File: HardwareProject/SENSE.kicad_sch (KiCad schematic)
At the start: 16 parts, among them U16 INA241A3xDDF, U17 INA241A3xDDF, U20 SGM8551XN, U21 SGM8551XN

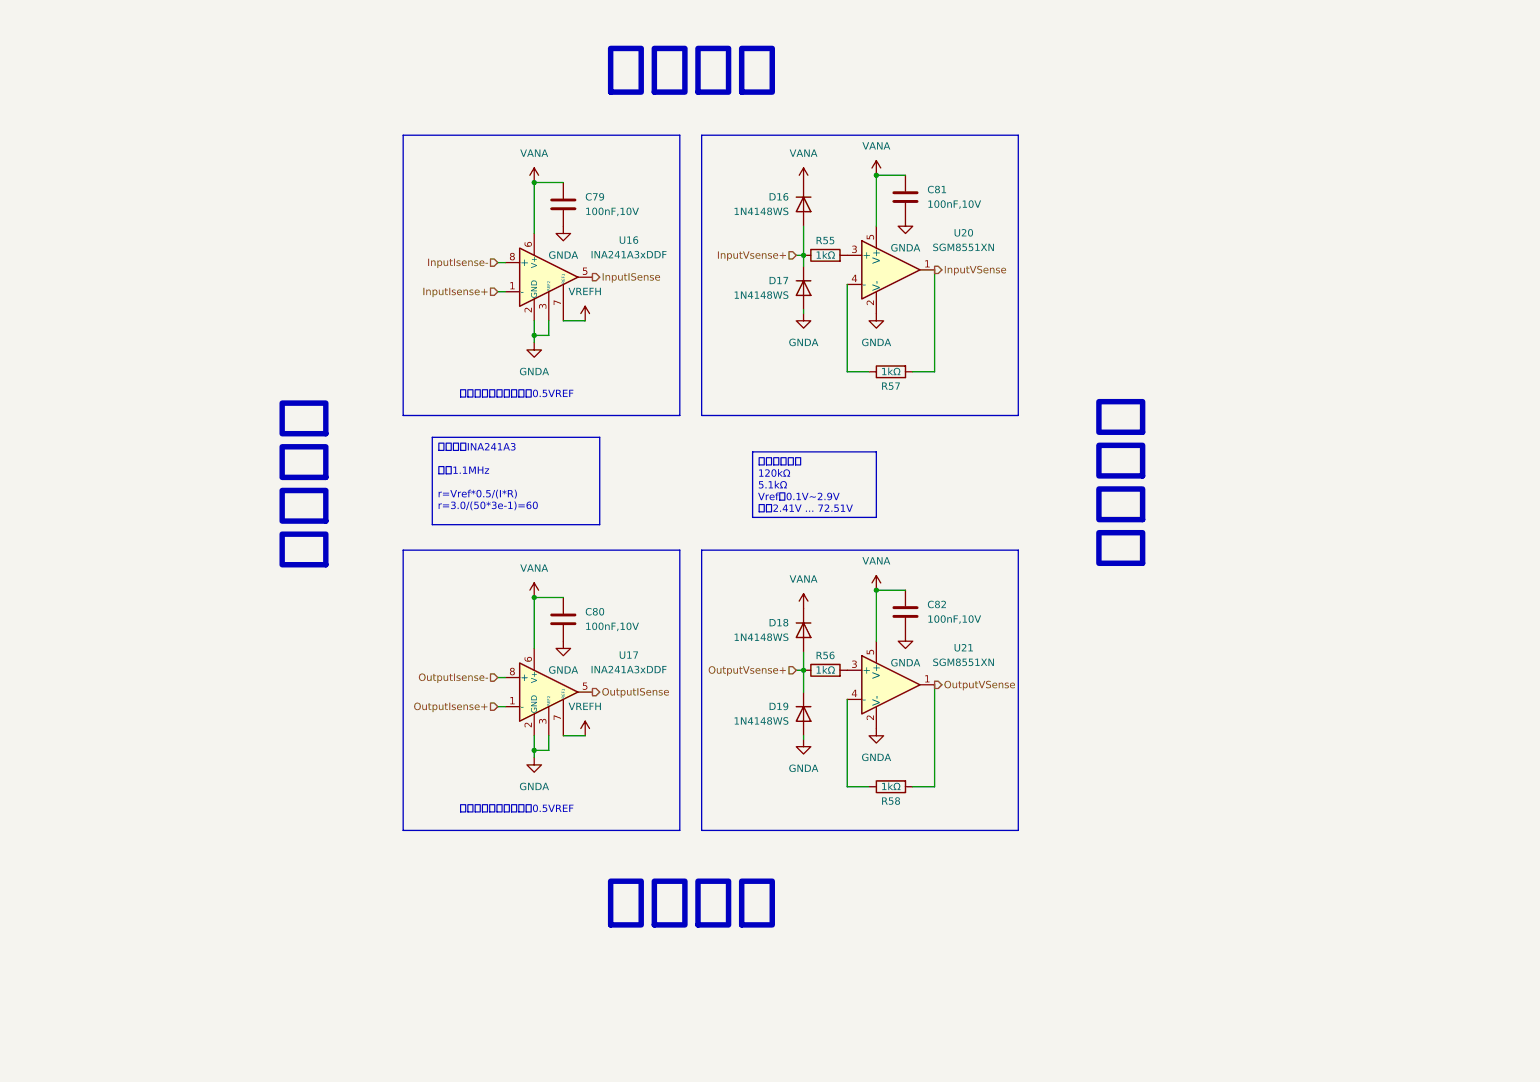
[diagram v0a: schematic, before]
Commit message: 修改了UCC27211A封装，此芯片此前的封装均错误 修改了采样线布局，为SAR ADC加入前置RC
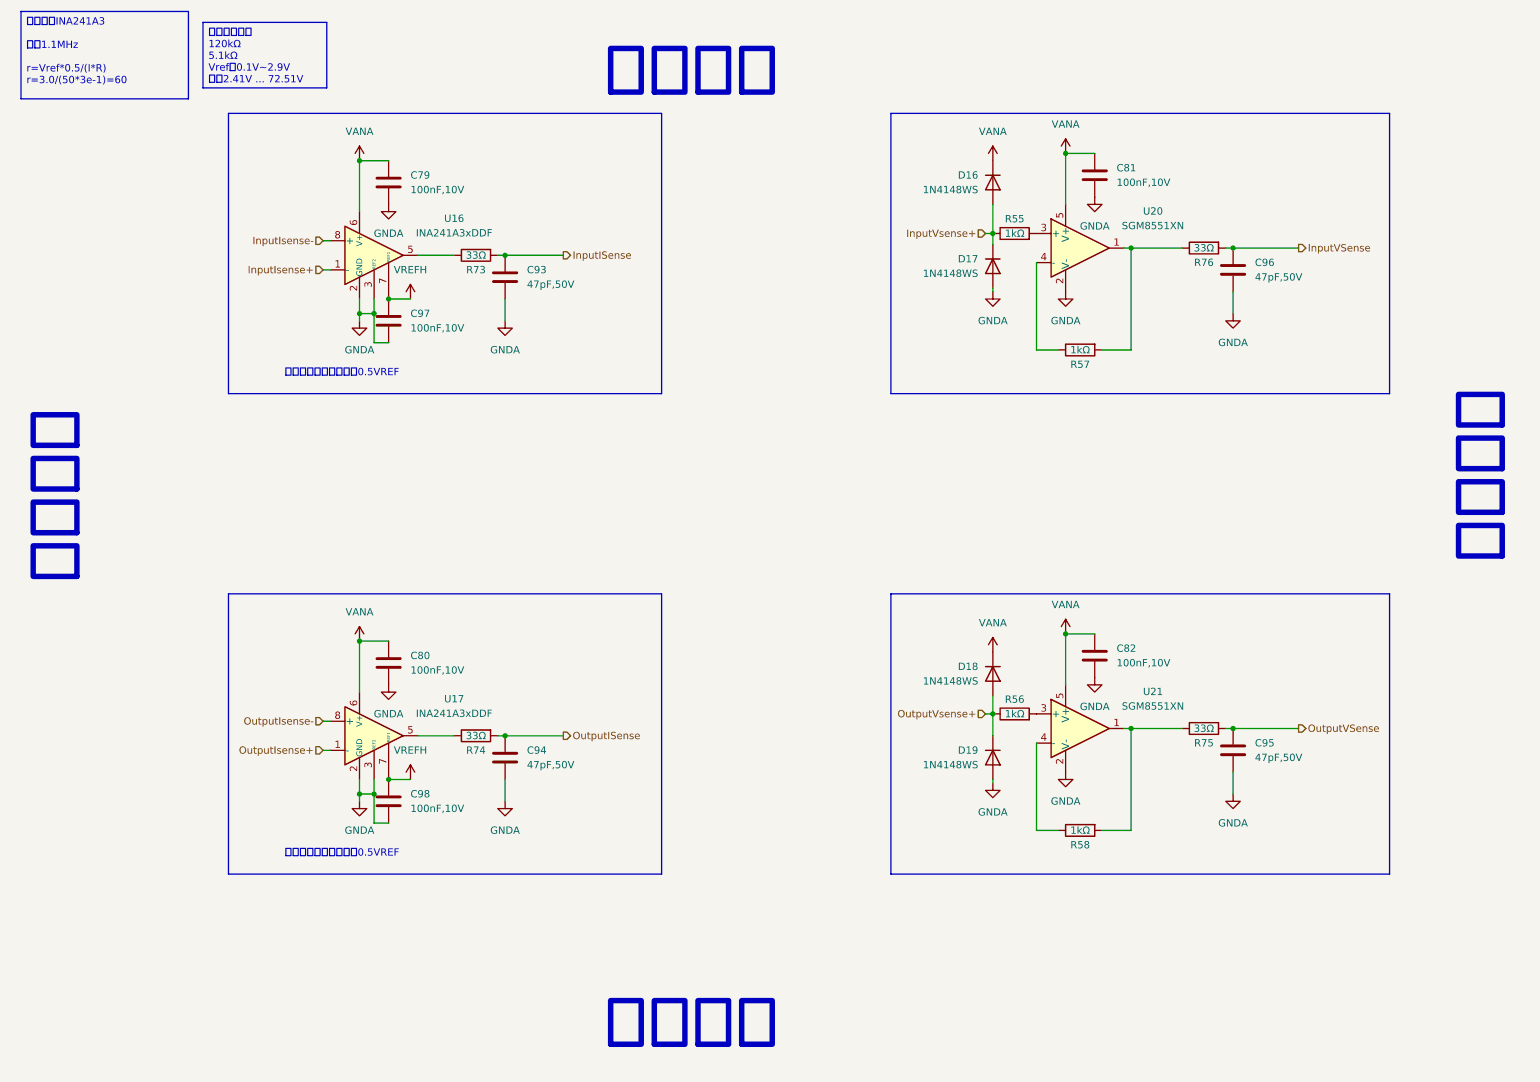
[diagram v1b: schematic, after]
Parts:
- added C93, C94, C95, C96: 47pF,50V, Capacitor_SMD:C_0603_1608Metric, symbol Device:C
- added C97, C98: 100nF,10V, Capacitor_SMD:C_0603_1608Metric, symbol Device:C
- added R73, R74, R75, R76: 33Ω, Resistor_SMD:R_0603_1608Metric, symbol Device:R
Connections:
- net GNDA: now also C93.2, C94.2, C95.2, C96.2, C97.2, C98.2
- net InputISense: now also C93.1, R73.2; no longer U16.5
- net InputVSense: now also C96.1, R76.2; no longer R57.2, U20.1
- net OutputISense: now also C94.1, R74.2; no longer U17.5
- net OutputVSense: now also C95.1, R75.2; no longer R58.2, U21.1
- net VREFH: now also C97.1, C98.1
- new net: R74.1, U17.5
- new net: R73.1, U16.5
- new net: R57.2, R76.1, U20.1
- new net: R58.2, R75.1, U21.1
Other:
- moved on the sheet: C79, C80, C81, C82, D16, D17, D18, D19, R55, R56, R57, R58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

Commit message: Rev3最终版本
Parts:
- added TP7, TP8: TestPoint_Probe, HPM6P41_BB:TestPoint_Bridge_Pitch1.2mm_Drill0.7mm, symbol Connector:TestPoint_Probe
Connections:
- net at R74.1, U17.5: now also TP8.1
- net at R73.1, U16.5: now also TP7.1
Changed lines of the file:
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@@
 	)
 	(junction
+		(at 90.17 57.15)
+		(diameter 0)
+		(color 0 0 0 0)
+	)
+	(junction
 		(at 78.74 67.31)
 		(diameter 0)
@@
 	)
 	(junction
+		(at 90.17 140.97)
+		(diameter 0)
+		(color 0 0 0 0)
+	)
+	(junction
 		(at 81.28 64.77)
 		(diameter 0)
@@
 	(wire
 		(pts
-			(xy 92.71 57.15) (xy 86.36 57.15)
+			(xy 92.71 57.15) (xy 90.17 57.15)
 		)
 		(stroke
@@
 	(wire
 		(pts
-			(xy 92.71 140.97) (xy 86.36 140.97)
+			(xy 92.71 140.97) (xy 90.17 140.97)
 		)
 		(stroke
@@
 	(wire
 		(pts
+			(xy 90.17 57.15) (xy 86.36 57.15)
+		)
+		(stroke
+			(width 0)
+			(type default)
+		)
+	)
+	(wire
+		(pts
 			(xy 69.85 59.69) (xy 71.12 59.69)
 		)
@@
 	(wire
 		(pts
+			(xy 90.17 140.97) (xy 86.36 140.97)
+		)
+		(stroke
+			(width 0)
+			(type default)
+		)
+	)
+	(wire
+		(pts
 			(xy 210.82 55.88) (xy 209.55 55.88)
 		)
@@
 	)
 	(symbol
+		(lib_id "Connector:TestPoint_Probe")
+		(at 90.17 140.97 270)
+		(unit 1)
+		(exclude_from_sim no)
+		(in_bom yes)
+		(on_board yes)
+		(dnp no)
+		(property "Reference" "TP8"
+			(at 93.0276 144.78 0)
+			(effects
+				(font
+					(size 1.27 1.27)
+				)
+				(justify left)
+			)
+		)
+		(property "Value" "TestPoint_Probe"
+			(at 90.4876 144.78 0)
+			(effects
+				(font
+					(size 1.27 1.27)
+				)
+				(justify left)
+				(hide yes)
+			)
+		)
+		(property "Footprint" "HPM6P41_BB:TestPoint_Bridge_Pitch1.2mm_Drill0.7mm"
+			(at 90.17 146.05 0)
+			(effects
+				(font
+					(size 1.27 1.27)
+				)
+				(hide yes)
+			)
+		)
+		(property "Datasheet" "~"
+			(at 90.17 146.05 0)
+			(effects
+				(font
+					(size 1.27 1.27)
+				)
+				(hide yes)
+			)
+		)
+		(property "Description" "test point (alternative probe-style design)"
+			(at 90.17 140.97 0)
+			(effects
+				(font
+					(size 1.27 1.27)
+				)
+				(hide yes)
+			)
+		)
+		(pin "1"
+		)
+		(instances
+			(project "HPM6P41_BB"
+				(path "/714b8a30-f9a7-49d4-a000-bc20c4884c7a/b4de388e-c979-411d-8cfc-9ded1b494090"
+					(reference "TP8")
+					(unit 1)
+				)
+			)
+		)
+	)
+	(symbol
 		(lib_id "Device:C")
 		(at 81.28 44.45 0)
@@
 					(unit 1)
 				)
+			)
+		)
+	)
+	(symbol
+		(lib_id "Connector:TestPoint_Probe")
+		(at 90.17 57.15 270)
+		(unit 1)
+		(exclude_from_sim no)
+		(in_bom yes)
+		(on_board yes)
+		(dnp no)
+		(property "Reference" "TP7"
+			(at 93.0276 60.96 0)
+			(effects
+				(font
+					(size 1.27 1.27)
+				)
+				(justify left)
+			)
+		)
+		(property "Value" "TestPoint_Probe"
+			(at 90.4876 60.96 0)
+			(effects
+				(font
+					(size 1.27 1.27)
+				)
+				(justify left)
+				(hide yes)
+			)
+		)
+		(property "Footprint" "HPM6P41_BB:TestPoint_Bridge_Pitch1.2mm_Drill0.7mm"
+			(at 90.17 62.23 0)
+			(effects
+				(font
+					(size 1.27 1.27)
+				)
+				(hide yes)
+			)
+		)
+		(property "Datasheet" "~"
+			(at 90.17 62.23 0)
+			(effects
+				(font
+					(size 1.27 1.27)
+				)
+				(hide yes)
+			)
+		)
+		(property "Description" "test point (alternative probe-style design)"
+			(at 90.17 57.15 0)
+			(effects
+				(font
+					(size 1.27 1.27)
+				)
+				(hide yes)
+			)
+		)
+		(pin "1"
+		)
+		(instances
+			(project "HPM6P41_BB"
+				(path "/714b8a30-f9a7-49d4-a000-bc20c4884c7a/b4de388e-c979-411d-8cfc-9ded1b494090"
+					(reference "TP7")
+					(unit 1)
+				)

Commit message: 换其他电感之前暂存一下
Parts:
- removed C80, C98: 100nF,10V, Capacitor_SMD:C_0603_1608Metric, symbol Device:C
- removed C94: 47pF,50V, Capacitor_SMD:C_0603_1608Metric, symbol Device:C
- removed R74: 33Ω, Resistor_SMD:R_0603_1608Metric, symbol Device:R
- removed TP8: TestPoint_Probe, HPM6P41_BB:TestPoint_Bridge_Pitch1.2mm_Drill0.7mm, symbol Connector:TestPoint_Probe
- removed U17: INA241A3xDDF, Package_TO_SOT_SMD:SOT-23-8, symbol Amplifier_Current:INA241A2xDDF
- TP7: footprint HPM6P41_BB:TestPoint_Bridge_Pitch1.2mm_Drill0.7mm -> HPM6P41_BB:测试点
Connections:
- net InputIsense+ renamed ISENSE-
- net InputIsense- renamed ISENSE+

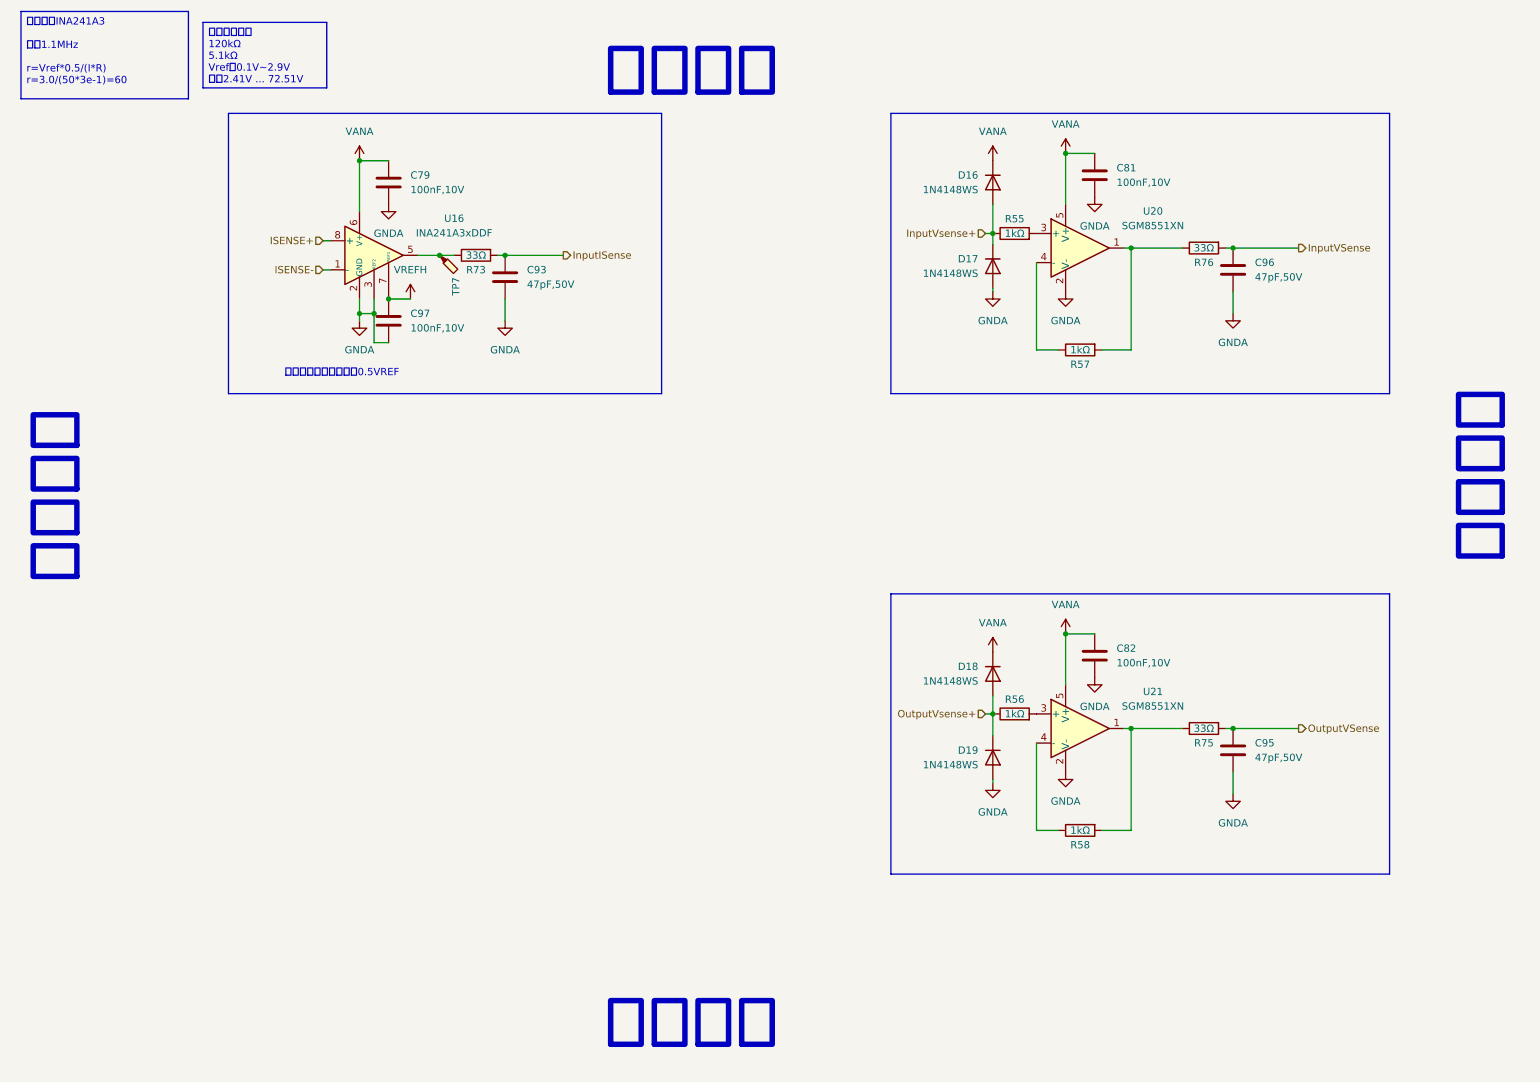
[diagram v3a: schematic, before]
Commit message: 完成Rev4 电源 驱动 模拟 IO
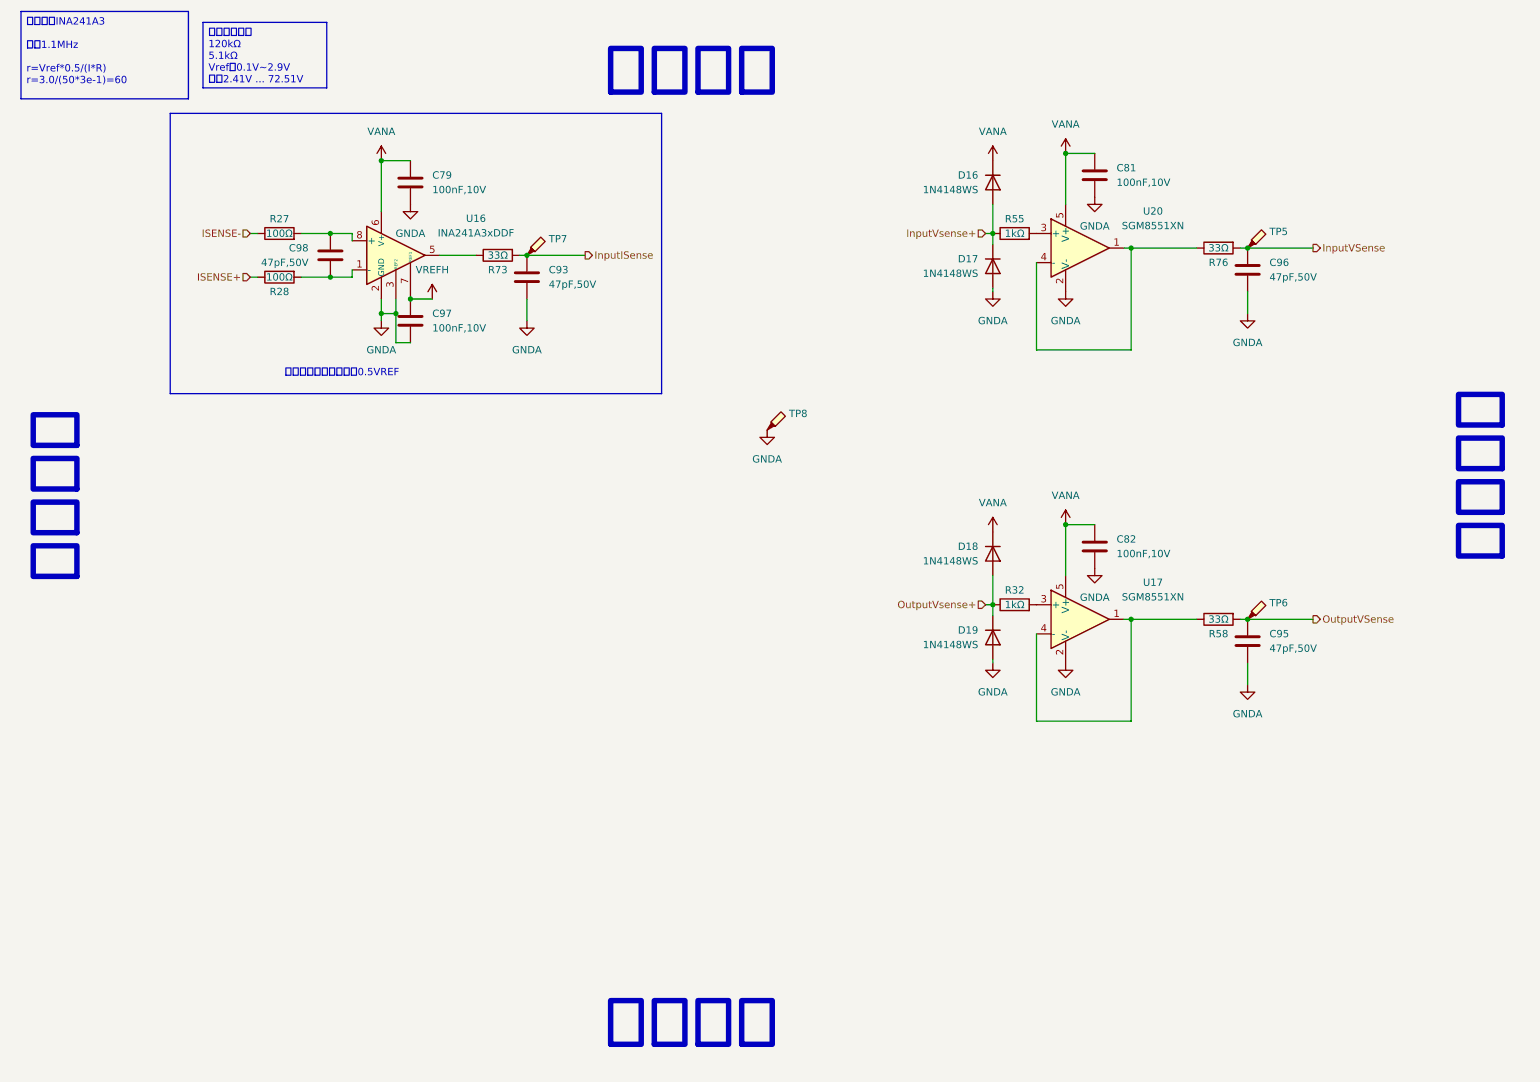
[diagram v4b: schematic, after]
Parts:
- removed R56, R57: 1kΩ, Resistor_SMD:R_0603_1608Metric, symbol Device:R
- removed R75: 33Ω, Resistor_SMD:R_0603_1608Metric, symbol Device:R
- removed U21: SGM8551XN, Package_TO_SOT_SMD:TSOT-23-5, symbol Amplifier_Operational:OPA188xxDBV
- added C98: 47pF,50V, Capacitor_SMD:C_0603_1608Metric, symbol Device:C
- added R27, R28: 100Ω, Resistor_SMD:R_0603_1608Metric, symbol Device:R
- added R32: 1kΩ, Resistor_SMD:R_0603_1608Metric, symbol Device:R
- added TP5, TP6, TP8: TestPoint_Probe, HPM6P41_BB:测试点, symbol Connector:TestPoint_Probe
- added U17: SGM8551XN, Package_TO_SOT_SMD:TSOT-23-5, symbol Amplifier_Operational:OPA188xxDBV
- D16, D17, D18, D19: footprint Diode_SMD:D_SOD-323 -> Diode_SMD:D_SOD-523
- R58: value 1kΩ -> 33Ω
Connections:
- net GNDA: now also TP8.1, U17.2 (V-)
- net ISENSE+: now also R28.1; no longer U16.8 (+)
- net ISENSE-: now also R27.1; no longer U16.1 (-)
- net InputISense: now also TP7.1
- net InputVSense: now also TP5.1
- net OutputVSense: now also R58.2, TP6.1
- net OutputVsense+: now also R32.1
- net VANA: now also U17.5 (V+)
- net at R73.1, U16.5: no longer TP7.1
- net at U20.4 (-): now also R76.1, U20.1
- net at R58.1: now also U17.1, U17.4 (-)
- new net: C98.2, R28.2, U16.1 (-)
- new net: C98.1, R27.2, U16.8 (+)
- new net: R32.2, U17.3 (+)
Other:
- moved on the sheet: C79, C93, C96, C97, R73, R76, TP7, U16

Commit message: rev4修改核心供电前保存（当前SYR838）
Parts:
- removed R32, R55: 1kΩ, Resistor_SMD:R_0603_1608Metric, symbol Device:R
- removed TP6: TestPoint_Probe, HPM6P41_BB:测试点, symbol Connector:TestPoint_Probe
- added C106, C109: 47pF,50V, Capacitor_SMD:C_0603_1608Metric, symbol Device:C
- added C107, C108: 100nF,50V, Capacitor_SMD:C_0603_1608Metric, symbol Device:C
- added R82, R83: 100Ω, Resistor_SMD:R_0603_1608Metric, symbol Device:R
- added R84: 33Ω, Resistor_SMD:R_0603_1608Metric, symbol Device:R
- added TP8, TP9: TestPoint_Probe, HPM6P41_BB:测试点, symbol Connector:TestPoint_Probe
- added U27: INA241A3xDDF, Package_TO_SOT_SMD:SOT-23-8, symbol Amplifier_Current:INA241A2xDDF
- C45: renamed from C79; value 100nF,10V -> 100nF,50V
- C46: renamed from C97; value 100nF,10V -> 100nF,50V
- C48: renamed from C81; value 100nF,10V -> 100nF,50V
- C49: renamed from C82; value 100nF,10V -> 100nF,50V
- renumbered C98 to C44, C93 to C47, C96 to C50, C95 to C51, D16 to D12, D17 to D13, D18 to D14, D19 to D15, R27 to R42, R28 to R43, R73 to R44, R76 to R47, R58 to R48, TP8 to TP6, U16 to U11, U20 to U12, U17 to U13
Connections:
- net GNDA: now also C107.2, C108.2, C109.2, U27.2 (GND), U27.3 (REF2), U27.4 (GND)
- net InputVSense: now also TP9.1; no longer TP5.1
- net InputVsense+: now also U12.3 (+)
- net OutputVSense: now also TP8.1
- net OutputVsense+: now also U13.3 (+)
- net VANA: now also C107.1, U27.6 (V+)
- net VREFH: now also C108.1, U27.7 (REF1)
- net InputISense renamed PeakSns
- net PeakSns: now also TP5.1; no longer TP7.1
- new net: C106.2, R83.2, U27.1 (-)
- new net: C106.1, R82.2, U27.8 (+)
- new net: R84.1, U27.5
- new net AvgSns: C109.1, R84.2, TP7.1
- new net IAvg+: R83.1
- new net IAvg-: R82.1
